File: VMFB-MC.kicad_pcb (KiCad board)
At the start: 2 copper layers, 64.6 x 67.3 mm, 49 parts, among them J1 Conn_01x04_Pin, J10 Conn_01x05_Pin, J2 Conn_01x04_Pin, J3 Conn_01x04_Pin, J4 Conn_01x02_Pin, J5 Conn_01x03_Pin, J6 Conn_01x04_Pin, J7 Conn_01x04_Pin, J8 Conn_01x04_Pin, J9 Conn_01x04_Pin, Q1 SFH313FA-2/3, Q2 SFH313FA-2/3, Q3 SFH313FA-2/3, Q4 SFH313FA-2/3, Q5 SFH313FA-2/3, Q6 SFH313FA-2/3, Q7 TIP120, Q8 TIP120, Q9 SFH313FA-2/3, U1 LM393

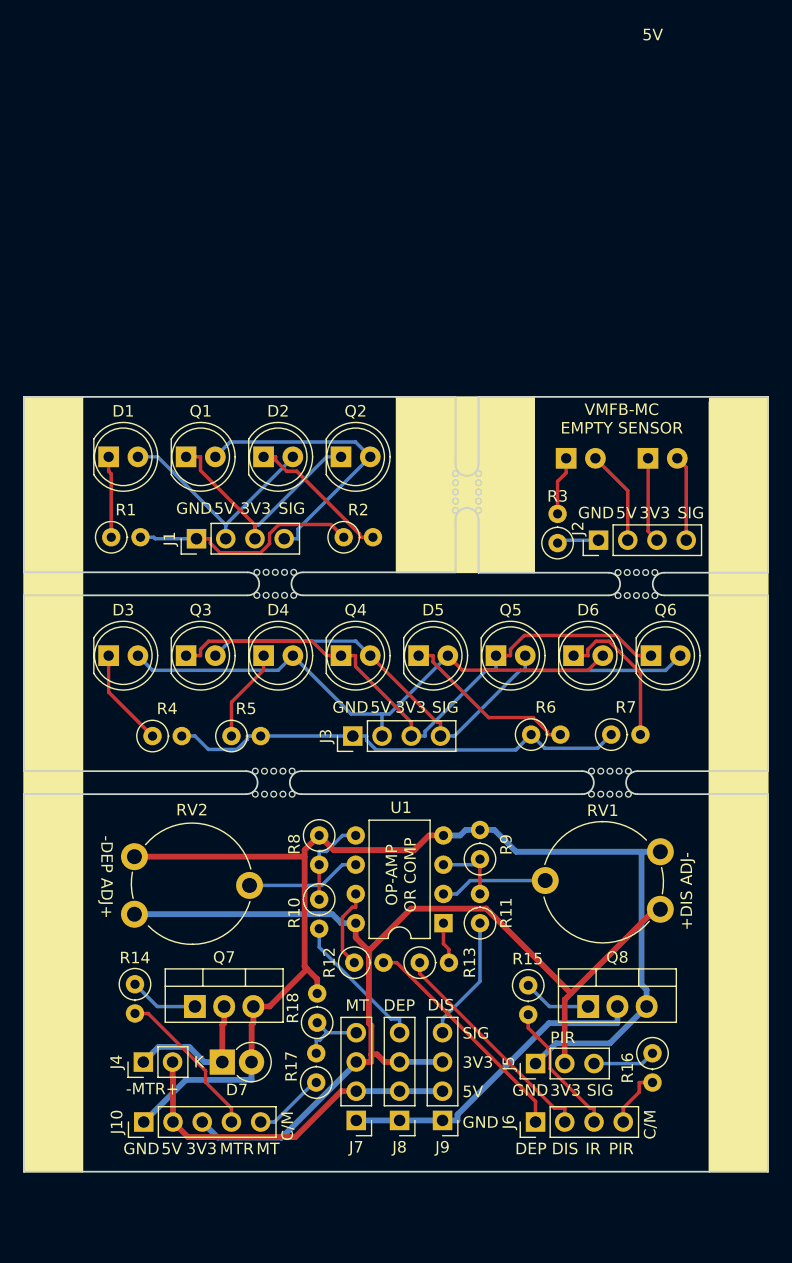
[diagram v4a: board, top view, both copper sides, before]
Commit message: clean up
removed some unnecessary components and revised component placement.
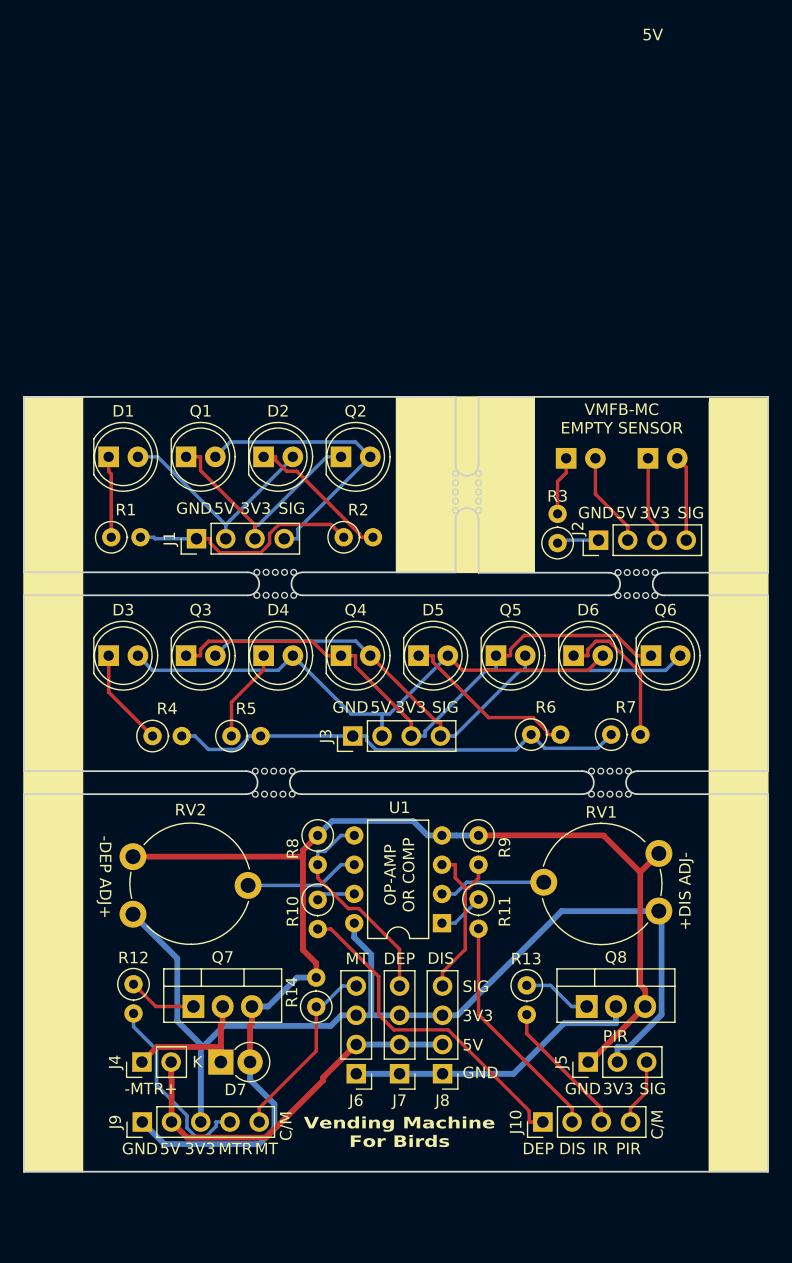
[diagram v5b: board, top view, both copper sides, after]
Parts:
- removed the R10 at (125.7, 93.7)
- removed the R11 at (139.7, 95.8)
- removed R16, R17: 10K, Resistor_THT:R_Axial_DIN0207_L6.3mm_D2.5mm_P2.54mm_Vertical
- moved R11 7.50 mm to (139.6, 93.7), turned to -90 degrees
- moved R10 6.32 mm to (125.6, 93.7), turned to -90 degrees
- moved J5 4.57 mm to (149.1, 107.8)
- moved J6 4.05 mm to (129.0, 108.8)
- moved J7 4.05 mm to (132.7, 108.8)
- moved J8 4.05 mm to (136.4, 108.8)
- moved R9 2.06 mm to (139.6, 88.1), turned to -90 degrees
- moved R14 1.38 mm to (125.5, 103.0)
- moved J10 0.63 mm to (145.2, 113.0)
- moved RV1 0.20 mm to (155.2, 89.7)
- moved G*** 0.13 mm to (132.6, 97.7)
- moved Q8 0.13 mm to (149.0, 103.0)
- moved R8 0.13 mm to (125.6, 88.1)
- moved U1 0.13 mm to (136.4, 95.8)
- moved D7 0.13 mm to (117.2, 107.8)
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- renumbered J6 to J10, J7 to J6, J8 to J7, J9 to J8, J10 to J9, R12 to R10, R13 to R11, R14 to R12, R15 to R13, R18 to R14
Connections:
- J5 pad 3: Net-(J5-Pin_3) -> PIR
- J6 pad 4: Net-(J7-Pin_4) -> EMPTY
- R11 pad 1: DISPENSE -> Net-(R11-Pad1)
- R11 pad 2: Net-(R13-Pad2) -> DISPENSE
- R14 pad 1: Net-(J7-Pin_4) -> EMPTY
- R8 pad 2: Net-(U1B-+) -> DEPOSIT SIG
- R9 pad 1: Net-(U1A-+) -> GND
- R9 pad 2: GND -> DISPENSE SIG
- U1 pad 1: Net-(R13-Pad2) -> Net-(R11-Pad1)
- U1 pad 3: Net-(U1A-+) -> DISPENSE SIG
- U1 pad 5: Net-(U1B-+) -> DEPOSIT SIG
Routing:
- net EMPTY: track 6.25 -> 16.3 mm
- net DEPOSIT: track 20.0 -> 29.0 mm
- net Net-(U1B-+): track 7.92 -> 0.00 mm
- net +3.3V: track 95.9 -> 89.2 mm
- net DEPOSIT SIG: track 12.4 -> 18.9 mm
- net Net-(U1A-+): track 6.39 -> 0.00 mm
- net Net-(J7-Pin_4): track 6.12 -> 0.00 mm
- net Net-(J5-Pin_3): track 5.45 -> 0.00 mm
- net DISPENSE SIG: track 10.9 -> 15.5 mm
- net Net-(R11-Pad1): track 0.00 -> 4.05 mm
- net Net-(R10-Pad1): track 7.04 -> 3.39 mm
- net Net-(R13-Pad2): track 3.63 -> 0.00 mm
- net MOTOR: track 13.6 -> 16.7 mm
- net IR GND: track 27.9 -> 25.8 mm
- net +5V: track 30.8 -> 32.8 mm
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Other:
- board text added: "Vending Machine For Birds"

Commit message: more clean up
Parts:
- moved R14 2.06 mm to (125.5, 101.0), turned to -90 degrees
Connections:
- R14 pad 1: EMPTY -> GND
- R14 pad 2: GND -> EMPTY
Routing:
- net GND: track 110.6 -> 0.00 mm
- net +3.3V: track 89.2 -> 0.00 mm
- net Net-(J3-Pin_3): track 51.5 -> 0.00 mm
- net Net-(J3-Pin_4): track 49.2 -> 0.00 mm
- net Net-(D3-A): track 48.6 -> 0.00 mm
- net Net-(J3-Pin_1): track 40.7 -> 0.00 mm
- net +5V: track 32.8 -> 0.00 mm
- net DEPOSIT: track 29.0 -> 0.00 mm
- net IR GND: track 25.8 -> 0.00 mm
- net Net-(J1-Pin_4): track 25.4 -> 0.00 mm
- net Net-(J1-Pin_3): track 21.5 -> 0.00 mm
- net Net-(J1-Pin_1): track 20.4 -> 0.00 mm
- net DISPENSE: track 20.2 -> 0.00 mm
- net Net-(D1-A): track 19.6 -> 0.00 mm
- net DEPOSIT SIG: track 18.9 -> 0.00 mm
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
